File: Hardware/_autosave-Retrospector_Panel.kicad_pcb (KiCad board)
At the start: 2 copper layers, 60.8 x 128.5 mm, 27 parts

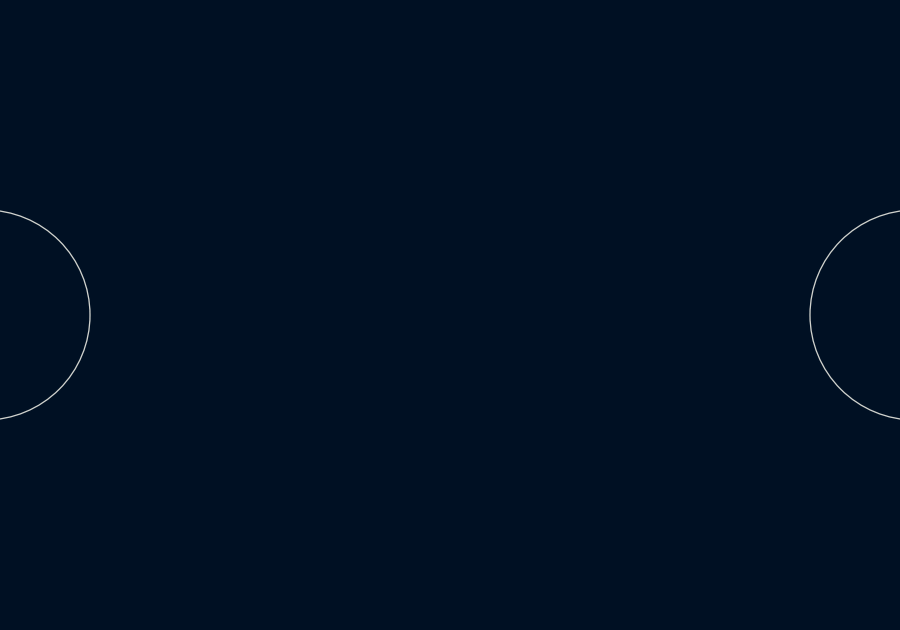
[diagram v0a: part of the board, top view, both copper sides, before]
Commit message: Final LED testing - decided on using Toshiba controller as WS2812B approach is very hacky and power inefficient
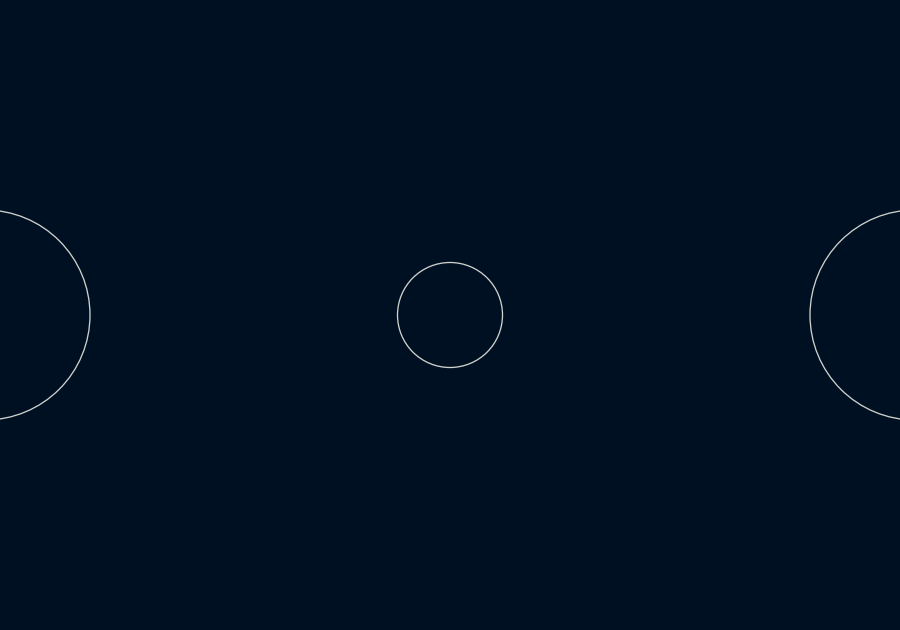
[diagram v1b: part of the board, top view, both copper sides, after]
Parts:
- added RESET: Subminiature_Switch, Custom_Footprints:Small_Pushbutton_Hole_3.5mm, B.Cu at (130.0, 64.5)
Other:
- board text added: "Link"
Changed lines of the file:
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@@
   (general
     (thickness 1.6)
-    (drawings 62)
+    (drawings 63)
     (tracks 0)
     (zones 0)
-    (modules 27)
+    (modules 28)
     (nets 1)
   )
@@
     (uvia_dia 0.3)
     (uvia_drill 0.1)
+  )
+  (module Custom_Footprints:Small_Pushbutton_Hole_3.5mm (layer B.Cu)
+    (at 130 64.5)
+    (descr "Button Hole 3.5mm")
+    (fp_text reference RESET (at 0 5.4) (layer B.SilkS) hide
+      (effects (font (size 1 1) (thickness 0.15)) (justify mirror))
+    )
+    (fp_text value Subminiature_Switch (at 0 -5.1) (layer B.Fab) hide
+      (effects (font (size 1 1) (thickness 0.15)) (justify mirror))
+    )
+    (fp_circle (center 0 0) (end 1.6 0) (layer B.CrtYd) (width 0.05))
+    (fp_circle (center 0 0) (end 1.5 0) (layer Cmts.User) (width 0.15))
+    (pad "" np_thru_hole circle (at 0 0) (size 3.5 3.5) (drill 3.5) (layers *.Cu *.Mask))
+    (model ${KISYS3DMOD}/Button_Switch_THT.3dshapes/SW_PUSH_6mm_H13mm.wrl
+      (offset (xyz -3.15 2.25 -11.5))
+      (scale (xyz 1 1 1))
+      (rotate (xyz 0 0 0))
+    )
   )
   (module Custom_Footprints:LED_Hole_3mm (layer B.Cu)
@@
     (pad "" np_thru_hole oval (at 0 0) (size 5 3.2) (drill oval 5 3.2) (layers *.Cu *.Mask))
   )
+  (gr_text Link (at 130 59.6) (layer B.Mask)
+    (effects (font (size 2 2) (thickness 0.3)) (justify mirror))
+  )
   (gr_text Wide (at 149.9 92.9) (layer B.Mask)
